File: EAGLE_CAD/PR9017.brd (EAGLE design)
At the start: 70 x 70 mm, 76 parts, among them SW1 C&K_PTS645, Y1 ABS25XTAL

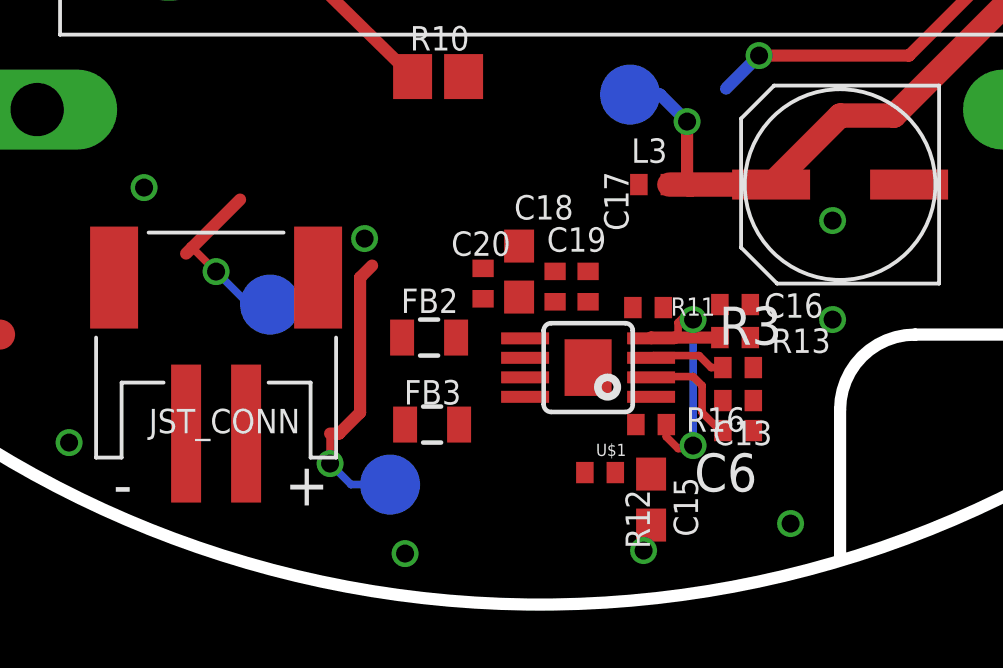
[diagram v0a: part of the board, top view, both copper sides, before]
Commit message: small amp changes
ripped up a few things.

the test pads on the speaker were at the wrong point (on the sch) so i
fixed that.

then rerouted most of the amp section. don’t love it, but it’s a start.
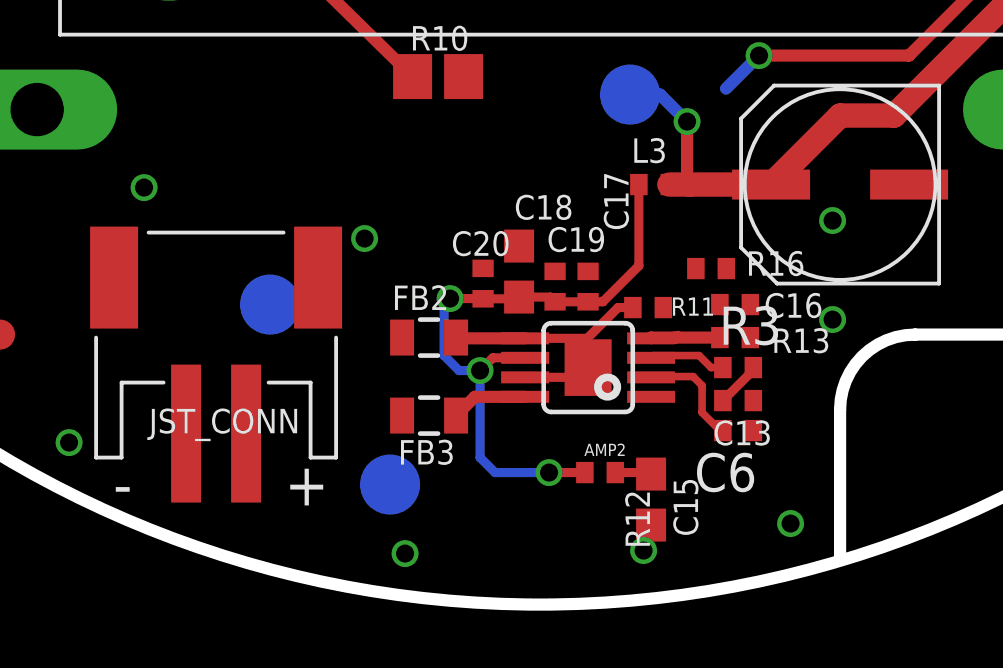
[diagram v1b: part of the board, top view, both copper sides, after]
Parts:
- moved R16 5.57 mm to (40.7, 11.2)
- moved FB3 0.32 mm to (31.3, 6.30)
- renumbered U$1 to AMP2
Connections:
- removed net N$17: FB2.2, JST_CONN.2
- removed net N$4: FB3.1, JST_CONN.1
- net A_IN: now also C13.1
- net A_OUT: no longer C13.1
- net SPK_OUT+: now also FB2.2, JST_CONN.2
- net SPK_OUT-: now also FB3.1, JST_CONN.1
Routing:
- net N$2: track 0.00 -> 21.3 mm, vias 0 -> 3
- net SPK_OUT-: track 9.65 -> 0.00 mm, vias 1 -> 0
- net N$5: track 9.16 -> 2.46 mm, vias 2 -> 0
- net N$11: track 0.00 -> 6.33 mm
- net SPK_OUT+: track 5.93 -> 0.00 mm, vias 1 -> 0
- net N$15: track 0.00 -> 2.56 mm
- net GND: track 8.34 -> 10.6 mm
- net N$3: track 0.00 -> 1.52 mm
- net N$20: track 0.00 -> 1.21 mm

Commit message: Updated Amp
Updated Amp SCH
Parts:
- removed C20: 100pf, PR_Parts_Library:C0402_WORTHINGTON
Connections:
- net GND: no longer C20.2
- net N$14: now also AMP2.4; no longer AMP2.3
- net N$2: no longer C20.1
- net N$5: now also AMP2.3; no longer AMP2.4
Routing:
- net N$4: track 6.33 -> 0.00 mm
- net N$2: track 21.3 -> 17.2 mm
- net N$11: track 2.56 -> 0.00 mm

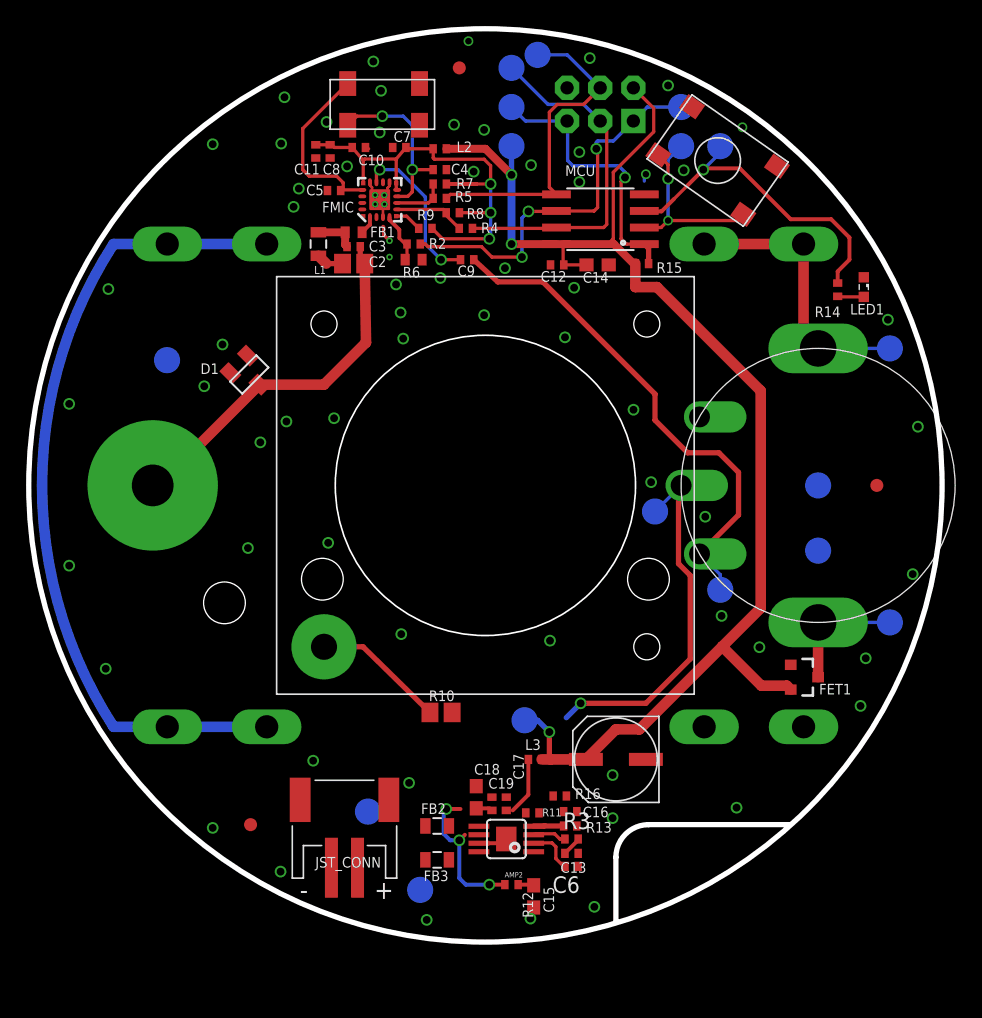
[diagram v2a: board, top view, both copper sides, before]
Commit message: Updated SCH
Updated the audio amp schematic with appropriate values for gain
setting resistors and input capacitors.
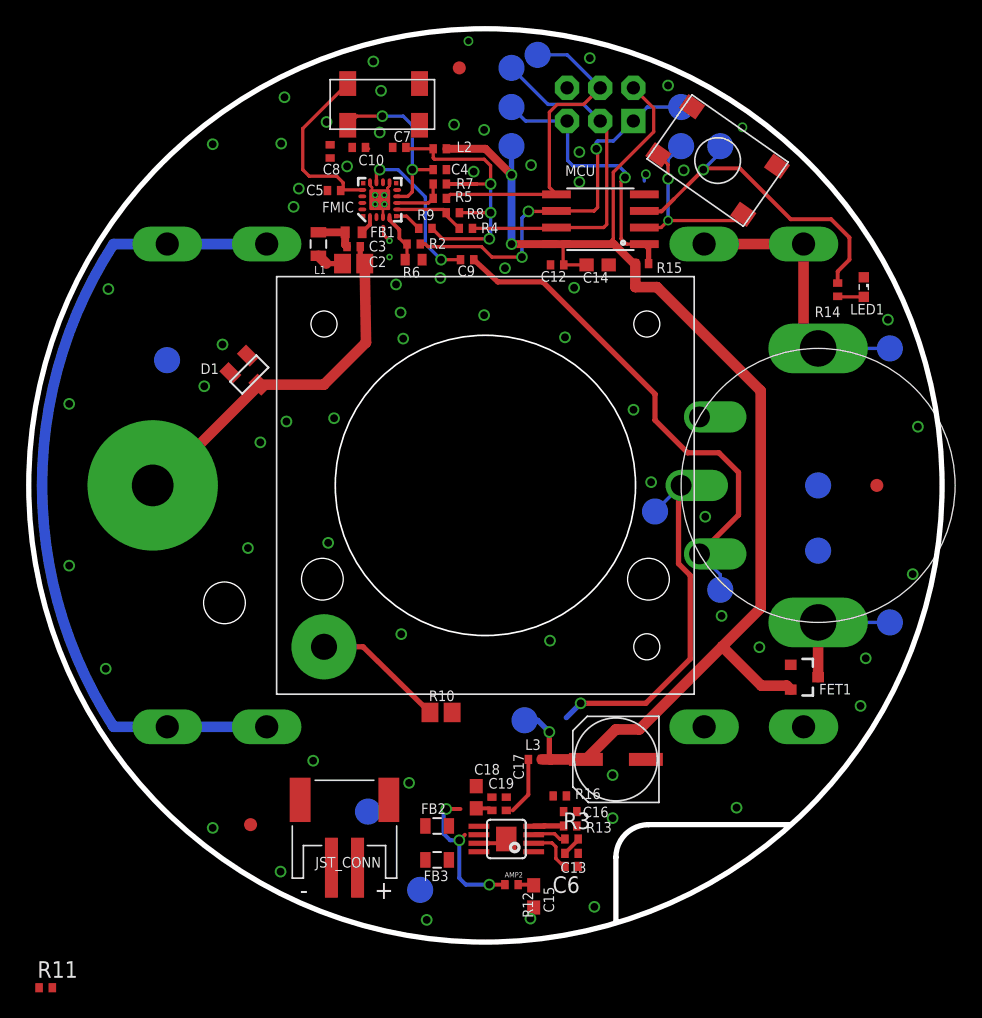
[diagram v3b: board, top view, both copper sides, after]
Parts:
- removed C11: .1u, PR_Parts_Library:C0402_WORTHINGTON
- R13, R3: value 40.2K -> 12K
- moved R11 39.6 mm to (1.30, -3.50), turned to 0 degrees
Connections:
- net 3.3V: no longer C11.1
- net GND: no longer C11.2
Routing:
- net 3.3V: track 38.0 -> 25.7 mm
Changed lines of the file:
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@@
 <attribute name="VALUE" x="24.741" y="55.63" size="0.762" layer="27" rot="R90"/>
 </element>
-<element name="R13" library="PR_Parts_Library" package="C0402_WORTHINGTON" value="40.2K" x="41.5" y="8.9" smashed="yes" rot="R180">
+<element name="R13" library="PR_Parts_Library" package="C0402_WORTHINGTON" value="12K" x="41.5" y="8.9" smashed="yes" rot="R180">
 <attribute name="NAME" x="42.711" y="8.389" size="0.8128" layer="25" font="vector" ratio="16"/>
 <attribute name="VALUE" x="42.389" y="10.932" size="1.27" layer="27" rot="R180"/>
@@
 <attribute name="NAME" x="25.265" y="59.535" size="0.8128" layer="25" font="vector" ratio="18"/>
 <attribute name="VALUE" x="24.665" y="58.995" size="1.27" layer="27"/>
-</element>
-<element name="C11" library="PR_Parts_Library" package="C0402_WORTHINGTON" value=".1u" x="22" y="60.6" smashed="yes" rot="R270">
-<attribute name="NAME" x="20.335" y="58.835" size="0.8128" layer="25" font="vector" ratio="16"/>
-<attribute name="VALUE" x="20.095" y="61.235" size="1.27" layer="27" rot="R270"/>
 </element>
 <element name="SW1" library="PR_Parts_Library" package="C&amp;K_TACTILE_SWITCH" value="C&amp;K_PTS645" x="52.8" y="59.9" rot="R325"/>
@@
 </element>
 <element name="C6" library="PR_Parts_Library" package="C0402_WORTHINGTON" value=".22uf" x="41.6" y="5.8" rot="R180"/>
-<element name="R3" library="PR_Parts_Library" package="C0402_WORTHINGTON" value="40.2K" x="41.6" y="7.9"/>
+<element name="R3" library="PR_Parts_Library" package="C0402_WORTHINGTON" value="12K" x="41.6" y="7.9"/>
 <element name="AMP2" library="PR_Parts_Library" package="POWER-SOP8" value="TPA6203A1" x="36.6" y="7.9" rot="R90"/>
-<element name="R11" library="PR_Parts_Library" package="C0402_WORTHINGTON" value="100K" x="38.6" y="9.9" smashed="yes" rot="R180">
-<attribute name="NAME" x="40.835" y="10.238" size="0.6096" layer="25" rot="R180"/>
-<attribute name="VALUE" x="39.235" y="11.805" size="1.27" layer="27" rot="R180"/>
-</element>
 <element name="R16" library="PR_Parts_Library" package="C0402_WORTHINGTON" value="100K" x="40.7" y="11.2" smashed="yes">
 <attribute name="NAME" x="41.865" y="10.962" size="0.8128" layer="25"/>
 <attribute name="VALUE" x="40.065" y="9.295" size="1.27" layer="27"/>
 </element>
+<element name="R11" library="PR_Parts_Library" package="C0402_WORTHINGTON" value="100K" x="1.3" y="-3.5"/>
 </elements>
 <signals>
@@
 <contactref element="C5" pad="2"/>
 <contactref element="C7" pad="2"/>
-<contactref element="C8" pad="2"/>
 <contactref element="R6" pad="1"/>
 <contactref element="C10" pad="2"/>
-<contactref element="C11" pad="2"/>
 <via x="28.7" y="46.25" extent="1-16" drill="0.6"/>
 <via x="26.41" y="67.49" extent="1-16" drill="0.6"/>
@@
 <contactref element="C18" pad="2"/>
 <contactref element="C19" pad="2"/>
+<contactref element="C8" pad="2"/>
 <wire x1="65.85" y1="47.7" x2="64" y2="50.95" width="0" layer="19" extent="1-1"/>
 <wire x1="68.15" y1="39.5" x2="65.85" y2="47.7" width="0" layer="19" extent="1-1"/>
@@
 <wire x1="24.4" y1="59.45" x2="26.15" y2="58.235" width="0" layer="19" extent="1-1"/>
 <wire x1="23.1" y1="60.0929" x2="24.4" y2="59.45" width="0" layer="19" extent="1-1"/>
-<wire x1="22" y1="60.0929" x2="23.1" y2="60.0929" width="0" layer="19" extent="1-1"/>
 <wire x1="25.8071" y1="60.9" x2="24.4" y2="59.45" width="0" layer="19" extent="1-1"/>
 <wire x1="26.9" y1="62.05" x2="26.05" y2="60.8" width="0" layer="19" extent="1-1"/>
@@
 <wire x1="20.3" y1="56.35" x2="20.7" y2="57.75" width="0" layer="19" extent="1-1"/>
 <wire x1="22.8254" y1="62.8548" x2="23.1" y2="60.0929" width="0" layer="19" extent="1-1"/>
-<wire x1="19.35" y1="61.2" x2="22" y2="60.0929" width="0" layer="19" extent="1-1"/>
 <wire x1="27" y1="65.25" x2="26.9" y2="62.05" width="0" layer="19" extent="1-1"/>
 <wire x1="26.41" y1="67.49" x2="27" y2="65.25" width="0" layer="19" extent="1-1"/>
+<wire x1="24.05" y1="52" x2="27.65" y2="52.5" width="0" layer="19" extent="1-1"/>
+<wire x1="19.35" y1="61.2" x2="20.7" y2="57.75" width="0" layer="19" extent="1-1"/>
 <wire x1="19.6" y1="64.75" x2="19.35" y2="61.2" width="0" layer="19" extent="1-1"/>
-<wire x1="24.05" y1="52" x2="27.65" y2="52.5" width="0" layer="19" extent="1-1"/>
 <wire x1="32.0071" y1="59.2" x2="27.8929" y2="60.9" width="0" layer="19" extent="1-1"/>
 <wire x1="34.1" y1="59.05" x2="32.0071" y2="59.2" width="0" layer="19" extent="1-1"/>
@@
 </signal>
 <signal name="3.3V">
-<contactref element="FMIC" pad="10"/>
-<contactref element="FMIC" pad="11"/>
-<contactref element="FMIC" pad="16"/>
 <contactref element="L2" pad="2"/>
-<contactref element="C7" pad="1"/>
-<contactref element="C8" pad="1"/>
 <contactref element="R8" pad="2"/>
 <contactref element="R9" pad="2"/>
 <contactref element="R7" pad="2"/>
-<contactref element="C10" pad="1"/>
-<contactref element="C11" pad="1"/>
-<wire x1="28.165" y1="58.165" x2="28.165" y2="57.72" width="0.254" layer="1"/>
-<wire x1="28.165" y1="57.72" x2="28.235" y2="57.65" width="0.254" layer="1"/>
 <wire x1="34.35" y1="58.1" x2="32.0071" y2="58.1" width="0.254" layer="1"/>
 <wire x1="31.7071" y1="53.9" x2="35.3" y2="53.9" width="0.254" layer="1"/>
@@
 <via x="35.4" y="58.1" extent="1-16" drill="0.6"/>
 <wire x1="35.4" y1="58.1" x2="35.4" y2="55.9" width="0.254" layer="16"/>
-<wire x1="28.165" y1="60.015" x2="28.9071" y2="60.9" width="0.254" layer="1"/>
-<wire x1="25.635" y1="58.165" x2="25.635" y2="59.915" width="0.254" layer="1"/>
-<wire x1="25.635" y1="59.915" x2="24.7929" y2="60.9" width="0.254" layer="1"/>
-<wire x1="28.165" y1="60.015" x2="25.735" y2="60.015" width="0.254" layer="1"/>
-<wire x1="25.735" y1="60.015" x2="25.635" y2="59.915" width="0.254" layer="1"/>
-<wire x1="28.165" y1="60.015" x2="28.165" y2="58.165" width="0.254" layer="1"/>
 <wire x1="33.0071" y1="55.9" x2="35.4" y2="55.9" width="0.254" layer="1"/>
 <wire x1="34.9" y1="60" x2="35.4" y2="59.5" width="0.254" layer="1"/>
 <wire x1="35.4" y1="59.5" x2="35.4" y2="58.1" width="0.254" layer="1"/>
 <wire x1="30.9929" y1="60.8" x2="29.15" y2="60.8" width="0.254" layer="1"/>
-<wire x1="29.15" y1="60.8" x2="28.9071" y2="60.9" width="0.254" layer="1"/>
-<wire x1="24.7929" y1="60.9" x2="23.45" y2="60.9" width="0.254" layer="1"/>
-<wire x1="23.45" y1="60.9" x2="23.1" y2="61.1071" width="0.254" layer="1"/>
-<wire x1="23.1" y1="61.1071" x2="22" y2="61.1071" width="0.254" layer="1"/>
 <wire x1="30.9071" y1="54.7" x2="31.7071" y2="53.9" width="0.254" layer="1"/>
 <wire x1="34.9" y1="60" x2="31.1" y2="60" width="0.254" layer="1"/>
@@
 <wire x1="31" y1="60.1" x2="31" y2="60.7929" width="0.254" layer="1"/>
 <wire x1="31" y1="60.7929" x2="30.9929" y2="60.8" width="0.254" layer="1"/>
+<contactref element="C7" pad="1"/>
+<contactref element="FMIC" pad="11"/>
+<contactref element="C10" pad="1"/>
+<contactref element="FMIC" pad="16"/>
+<contactref element="FMIC" pad="10"/>
+<contactref element="C8" pad="1"/>
+<wire x1="29.15" y1="60.8" x2="28.9071" y2="60.9" width="0" layer="19" extent="1-1"/>
+<wire x1="28.165" y1="58.165" x2="29.15" y2="60.8" width="0" layer="19" extent="1-1"/>
+<wire x1="28.235" y1="57.65" x2="28.165" y2="58.165" width="0" layer="19" extent="1-1"/>
+<wire x1="25.635" y1="58.165" x2="28.165" y2="58.165" width="0" layer="19" extent="1-1"/>
+<wire x1="24.7929" y1="60.9" x2="25.635" y2="58.165" width="0" layer="19" extent="1-1"/>
+<wire x1="23.1" y1="61.1071" x2="24.7929" y2="60.9" width="0" layer="19" extent="1-1"/>
 </signal>
 <signal name="VCC">
@@
 <signal name="N$14">
 <contactref element="R3" pad="1"/>
-<contactref element="R11" pad="1"/>
 <wire x1="41.0929" y1="7.9" x2="40.7" y2="7.9" width="0.254" layer="1"/>
 <wire x1="40.7" y1="7.9" x2="40.3" y2="8.3" width="0.254" layer="1"/>
 <wire x1="40.3" y1="8.3" x2="38.775" y2="8.3" width="0.254" layer="1"/>
 <contactref element="AMP2" pad="4"/>
-<wire x1="38.7" y1="8.875" x2="39.1071" y2="9.9" width="0" layer="19" extent="1-1"/>
-<wire x1="38.775" y1="8.3" x2="38.7" y2="8.875" width="0" layer="19" extent="1-1"/>
+<contactref element="R11" pad="1"/>
+<wire x1="38.7" y1="8.875" x2="38.775" y2="8.3" width="0" layer="19" extent="1-1"/>
+<wire x1="0.7929" y1="-3.5" x2="38.775" y2="8.3" width="0" layer="19" extent="1-1"/>
 </signal>
 <signal name="N$2">
@@
 <signal name="N$4">
 <contactref element="AMP2" pad="5"/>
+<contactref element="FB2" pad="1"/>
 <contactref element="R11" pad="2"/>
-<contactref element="FB2" pad="1"/>
-<wire x1="34.5" y1="8.875" x2="38.0929" y2="9.9" width="0" layer="19" extent="1-1"/>
 <wire x1="32.2" y1="8.9" x2="34.5" y2="8.875" width="0" layer="19" extent="1-1"/>
+<wire x1="1.8071" y1="-3.5" x2="32.2" y2="8.9" width="0" layer="19" extent="1-1"/>
 </signal>
 <signal name="N$11">
